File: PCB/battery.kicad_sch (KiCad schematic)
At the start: 1 part

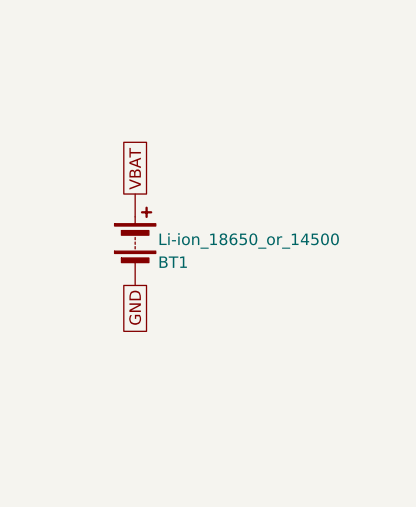
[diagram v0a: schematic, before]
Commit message: Fix footprints and begin layout (#17)
* refactor: updated gulikit footprint

This updates the gulikit thumbstick footprint to be accurate.

* layout: beginning pcb layout

This updates the schematic with a few different footprints while also starts the layout.
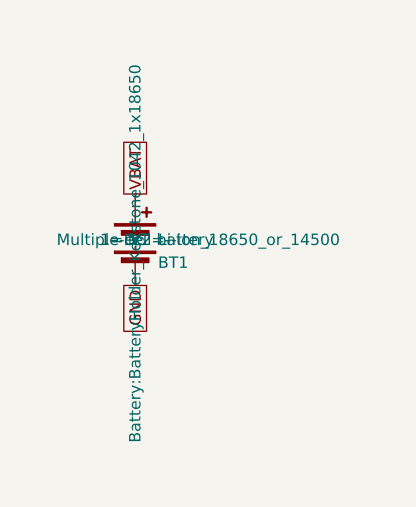
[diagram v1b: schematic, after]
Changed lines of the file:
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@@
 		(property "Footprint" "Battery:BatteryHolder_Keystone_1042_1x18650"
 			(at 148.59 106.934 90)
-			(hide yes)
 			(show_name no)
 			(do_not_autoplace no)
@@
 		(property "Datasheet" ""
 			(at 148.59 106.934 90)
-			(hide yes)
 			(show_name no)
 			(do_not_autoplace no)
@@
 		(property "Description" "Multiple-cell battery"
 			(at 148.59 105.41 0)
-			(hide yes)
 			(show_name no)
 			(do_not_autoplace no)
@@
 		(property "Sim.Device" "V"
 			(at 148.59 105.41 0)
-			(hide yes)
 			(show_name no)
 			(do_not_autoplace no)
@@
 		(property "Sim.Type" "DC"
 			(at 148.59 105.41 0)
-			(hide yes)
 			(show_name no)
 			(do_not_autoplace no)
@@
 		(property "Sim.Pins" "1=+ 2=-"
 			(at 148.59 105.41 0)
-			(hide yes)
 			(show_name no)
 			(do_not_autoplace no)
@@
 		(instances
 			(project "snips_controller"
-				(path "/868f8289-8434-4465-b2f4-2accc5e40bab/748cb1dd-d7df-4e73-a93b-27e67a5ba349"
+				(path "/868f8289-8434-4465-b2f4-2accc5e40bab/1c35c5cf-c022-4f34-b463-7ba7d15d3ffa"
 					(reference "BT1")
 					(unit 1)
+				)
+			)
+			(project ""
+				(path "/d0f5b7d7-b2b6-4492-958c-e60265d3c6b4/1c35c5cf-c022-4f34-b463-7ba7d15d3ffa"
+					(reference "BT1")
+					(unit 1)

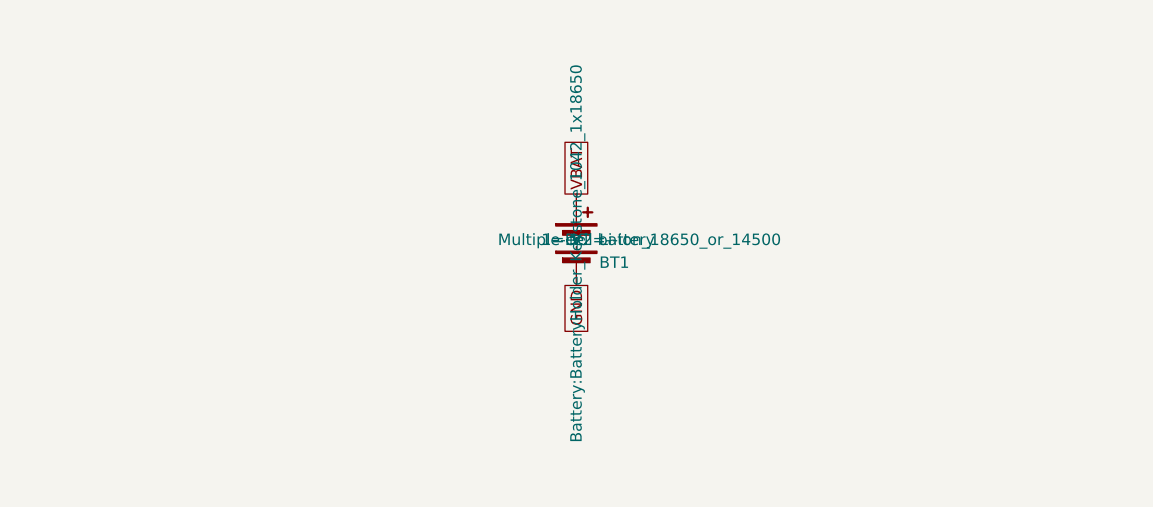
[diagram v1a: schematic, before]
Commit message: refactor: swap footprints and add symmetry
This updates the footprints of a couple components to be smaller and closer to what we want. It also adds two buttons to ensure left and right side symmetry.
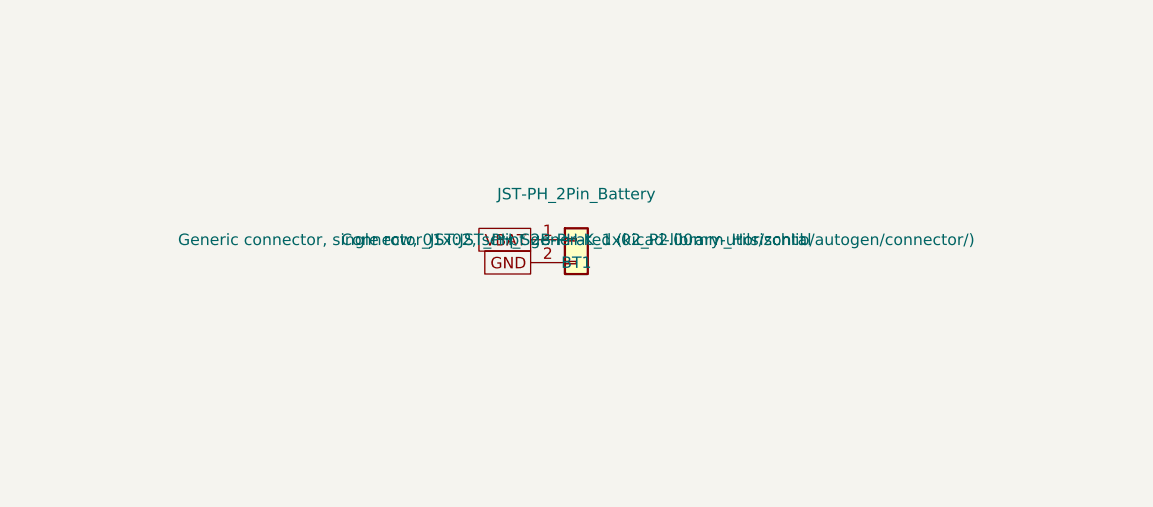
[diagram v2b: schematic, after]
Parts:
- removed BT1: Li-ion_18650_or_14500, Battery:BatteryHolder_Keystone_1042_1x18650, symbol Device:Battery
- added BT1: JST-PH_2Pin_Battery, Connector_JST:JST_PH_S2B-PH-K_1x02_P2.00mm_Horizontal, symbol Connector_Generic:Conn_01x02
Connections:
- net GND: now also BT1.2 (Pin_2)
- net VBAT: now also BT1.1 (Pin_1)
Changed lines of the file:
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@@
 	(generator_version "10.0")
 	(paper "A4")
-	(global_label "VBAT"
+	(global_label "GND"
 		(shape passive)
-		(at 148.59 100.33 90)
+		(at 143.51 107.95 180)
 		(fields_autoplaced yes)
 		(effects
@@
 				(size 1.27 1.27)
 			)
-			(justify left)
+			(justify right)
 		)
 		(property "Intersheetrefs" "${INTERSHEET_REFS}"
-			(at 148.59 100.33 0)
+			(at 143.51 107.95 0)
 			(hide yes)
 			(show_name no)
@@
 		)
 	)
-	(global_label "GND"
+	(global_label "VBAT"
 		(shape passive)
-		(at 148.59 110.49 270)
+		(at 143.51 105.41 180)
 		(fields_autoplaced yes)
 		(effects
@@
 		)
 		(property "Intersheetrefs" "${INTERSHEET_REFS}"
-			(at 148.59 110.49 0)
+			(at 143.51 105.41 0)
 			(hide yes)
 			(show_name no)
@@
 	)
 	(symbol
-		(lib_id "Device:Battery")
+		(lib_id "Connector_Generic:Conn_01x02")
 		(at 148.59 105.41 0)
 		(unit 1)
@@
 		(fields_autoplaced yes)
 		(property "Reference" "BT1"
-			(at 151.13 107.95 0)
+			(at 148.59 107.95 0)
 			(show_name no)
 			(do_not_autoplace no)
@@
 					(size 1.27 1.27)
 				)
-				(justify left)
 			)
 		)
-		(property "Value" "Li-ion_18650_or_14500"
-			(at 151.13 105.41 0)
+		(property "Value" "JST-PH_2Pin_Battery"
+			(at 148.59 100.33 0)
 			(show_name no)
 			(do_not_autoplace no)
@@
 					(size 1.27 1.27)
 				)
-				(justify left)
 			)
 		)
-		(property "Footprint" "Battery:BatteryHolder_Keystone_1042_1x18650"
-			(at 148.59 106.934 90)
+		(property "Footprint" "Connector_JST:JST_PH_S2B-PH-K_1x02_P2.00mm_Horizontal"
+			(at 148.59 105.41 0)
 			(show_name no)
 			(do_not_autoplace no)
@@
 		)
 		(property "Datasheet" ""
-			(at 148.59 106.934 90)
-			(show_name no)
-			(do_not_autoplace no)
-			(effects
-				(font
-					(size 1.27 1.27)
-				)
-			)
-		)
-		(property "Description" "Multiple-cell battery"
 			(at 148.59 105.41 0)
 			(show_name no)
@@
 			)
 		)
-		(property "Sim.Device" "V"
-			(at 148.59 105.41 0)
-			(show_name no)
-			(do_not_autoplace no)
-			(effects
-				(font
-					(size 1.27 1.27)
-				)
-			)
-		)
-		(property "Sim.Type" "DC"
-			(at 148.59 105.41 0)
-			(show_name no)
-			(do_not_autoplace no)
-			(effects
-				(font
-					(size 1.27 1.27)
-				)
-			)
-		)
-		(property "Sim.Pins" "1=+ 2=-"
+		(property "Description" "Generic connector, single row, 01x02, script generated (kicad-library-utils/schlib/autogen/connector/)"
 			(at 148.59 105.41 0)
 			(show_name no)
@@
 		(instances
 			(project "snips_controller"
-				(path "/868f8289-8434-4465-b2f4-2accc5e40bab/1c35c5cf-c022-4f34-b463-7ba7d15d3ffa"
+				(path "/f9d779c6-e1a6-4677-9004-6e9cc3d2fa8d/4f9b61d4-6d11-4d2d-a5a2-c90e20b99588"
 					(reference "BT1")
 					(unit 1)
-				)
-			)
-			(project ""
-				(path "/d0f5b7d7-b2b6-4492-958c-e60265d3c6b4/1c35c5cf-c022-4f34-b463-7ba7d15d3ffa"
-					(reference "BT1")
-					(unit 1)

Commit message: task: part number populated (#26)
kicad-happy run part 2 - MPN numbers populated
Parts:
- BT1: MF (none) -> JST; Manufacturer_Part_Number (none) -> S2B-PH-K
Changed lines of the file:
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@@
+			)
+		)
+		(property "MF" "JST" (at 0 0 0)
+			(effects
+				(font
+					(size 1.27 1.27)
+				)
+				(hide yes)
+			)
+		)
+		(property "Manufacturer_Part_Number" "S2B-PH-K" (at 0 0 0)
+			(effects
+				(font
+					(size 1.27 1.27)
+				)
+				(hide yes)
 			)
 		)

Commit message: task: more gerbers
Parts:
- BT1: Manufacturer_Part_Number S2B-PH-K -> S2B-PH-K(LF)(SN)
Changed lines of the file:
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@@
 			)
 		)
-		(property "Manufacturer_Part_Number" "S2B-PH-K"
+		(property "Manufacturer_Part_Number" "S2B-PH-K(LF)(SN)"
 			(at 0 0 0)
 			(hide yes)
